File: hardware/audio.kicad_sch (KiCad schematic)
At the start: 21 parts, among them J4 3.5mm stereo, U50 MCP6002

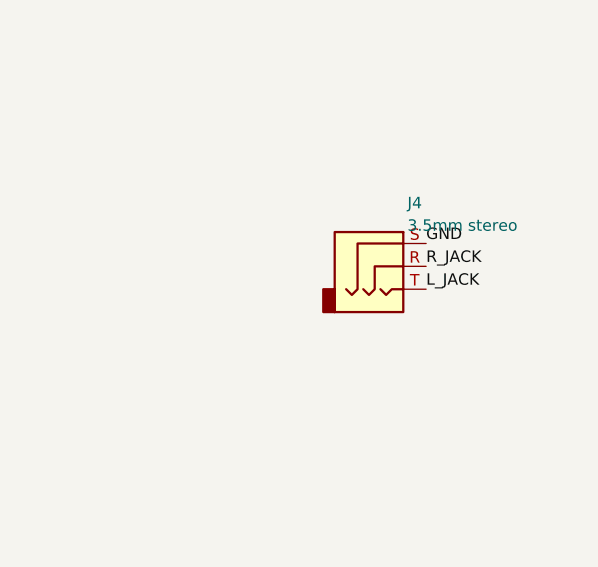
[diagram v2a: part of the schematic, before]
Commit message: BOM cost optimisation against the JLCPCB catalog; schematic-side regulator fix
jlc_price.py prices the BOM via JLCPCB's parts API. Substitutions cut parts+fees
per board from $32.95 to $17.19 on a 10-board run: PSRAM DNP, electrolytic bulk
caps, TF-01A socket, PJ-320D jack, 74HC574, GD25Q128E, 0603 10 uF, basic LED,
preferred MCP6002; U16 decoder deleted (strobes on GPIO), U8 and U15 become
74LVC245s; J3/J5 hand-soldered. Adds the AOTA inductor and VREG_AVDD filter.
PCB needs a relayout; fab/ is stale.

Co-Authored-By: Claude Fable 5.1 <noreply@anthropic.com>
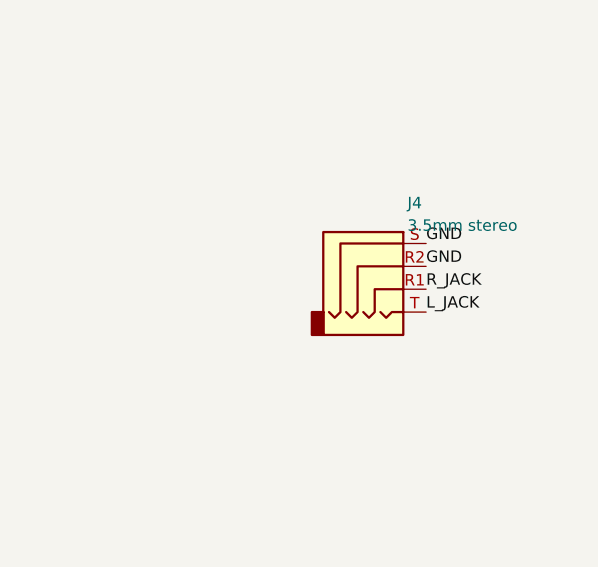
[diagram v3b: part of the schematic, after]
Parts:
- removed J4: 3.5mm stereo, Connector_Audio:Jack_3.5mm_CUI_SJ-3523-SMT_Horizontal, symbol Connector_Audio:AudioJack3
- added J4: 3.5mm stereo, Connector_Audio:Jack_3.5mm_PJ320D_Horizontal, symbol Connector_Audio:AudioJack4
- C80, C81: footprint Capacitor_SMD:C_0805_2012Metric -> Capacitor_SMD:C_0603_1608Metric; LCSC C15850 -> C19702; MPN CL21A106KAYNNNE -> CL10A106KP8NNNC
- U50: LCSC C125816 -> C7377; MPN MCP6002T-E/SN -> MCP6002T-I/SN
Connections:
- net GND: now also J4.R2, J4.S
- net L_JACK: now also J4.T
- net R_JACK: now also J4.R1
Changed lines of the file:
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@@
     (property "Datasheet" "" (at 199.39 110.49 0) (effects (font (size 1.27 1.27)) (justify left) (hide yes)))
     (property "Description" "" (at 199.39 110.49 0) (effects (font (size 1.27 1.27)) (justify left) (hide yes)))
-    (property "MPN" "MCP6002T-E/SN" (at 199.39 110.49 0) (effects (font (size 1.27 1.27)) (justify left) (hide yes)))
-    (property "LCSC" "C125816" (at 199.39 110.49 0) (effects (font (size 1.27 1.27)) (justify left) (hide yes)))
+    (property "MPN" "MCP6002T-I/SN" (at 199.39 110.49 0) (effects (font (size 1.27 1.27)) (justify left) (hide yes)))
+    (property "LCSC" "C7377" (at 199.39 110.49 0) (effects (font (size 1.27 1.27)) (justify left) (hide yes)))
     (pin "1")
     (pin "2")
@@
     (property "Datasheet" "" (at 199.39 170.18 0) (effects (font (size 1.27 1.27)) (justify left) (hide yes)))
     (property "Description" "" (at 199.39 170.18 0) (effects (font (size 1.27 1.27)) (justify left) (hide yes)))
-    (property "MPN" "MCP6002T-E/SN" (at 199.39 170.18 0) (effects (font (size 1.27 1.27)) (justify left) (hide yes)))
-    (property "LCSC" "C125816" (at 199.39 170.18 0) (effects (font (size 1.27 1.27)) (justify left) (hide yes)))
+    (property "MPN" "MCP6002T-I/SN" (at 199.39 170.18 0) (effects (font (size 1.27 1.27)) (justify left) (hide yes)))
+    (property "LCSC" "C7377" (at 199.39 170.18 0) (effects (font (size 1.27 1.27)) (justify left) (hide yes)))
     (pin "1")
     (pin "2")
@@
     (property "Datasheet" "" (at 199.39 229.87 0) (effects (font (size 1.27 1.27)) (justify left) (hide yes)))
     (property "Description" "" (at 199.39 229.87 0) (effects (font (size 1.27 1.27)) (justify left) (hide yes)))
-    (property "MPN" "MCP6002T-E/SN" (at 199.39 229.87 0) (effects (font (size 1.27 1.27)) (justify left) (hide yes)))
-    (property "LCSC" "C125816" (at 199.39 229.87 0) (effects (font (size 1.27 1.27)) (justify left) (hide yes)))
+    (property "MPN" "MCP6002T-I/SN" (at 199.39 229.87 0) (effects (font (size 1.27 1.27)) (justify left) (hide yes)))
+    (property "LCSC" "C7377" (at 199.39 229.87 0) (effects (font (size 1.27 1.27)) (justify left) (hide yes)))
     (pin "1")
     (pin "2")
@@
     (property "Reference" "C80" (at 253.19 102.18 0) (effects (font (size 1.27 1.27)) (justify left)))
     (property "Value" "10u" (at 253.19 104.68 0) (effects (font (size 1.27 1.27)) (justify left)))
-    (property "Footprint" "Capacitor_SMD:C_0805_2012Metric" (at 250.19 110.49 0) (effects (font (size 1.27 1.27)) (justify left) (hide yes)))
+    (property "Footprint" "Capacitor_SMD:C_0603_1608Metric" (at 250.19 110.49 0) (effects (font (size 1.27 1.27)) (justify left) (hide yes)))
     (property "Datasheet" "" (at 250.19 110.49 0) (effects (font (size 1.27 1.27)) (justify left) (hide yes)))
     (property "Description" "" (at 250.19 110.49 0) (effects (font (size 1.27 1.27)) (justify left) (hide yes)))
-    (property "MPN" "CL21A106KAYNNNE" (at 250.19 110.49 0) (effects (font (size 1.27 1.27)) (justify left) (hide yes)))
-    (property "LCSC" "C15850" (at 250.19 110.49 0) (effects (font (size 1.27 1.27)) (justify left) (hide yes)))
+    (property "MPN" "CL10A106KP8NNNC" (at 250.19 110.49 0) (effects (font (size 1.27 1.27)) (justify left) (hide yes)))
+    (property "LCSC" "C19702" (at 250.19 110.49 0) (effects (font (size 1.27 1.27)) (justify left) (hide yes)))
     (pin "1")
     (pin "2")
@@
     (property "Reference" "C81" (at 253.19 161.87 0) (effects (font (size 1.27 1.27)) (justify left)))
     (property "Value" "10u" (at 253.19 164.37 0) (effects (font (size 1.27 1.27)) (justify left)))
-    (property "Footprint" "Capacitor_SMD:C_0805_2012Metric" (at 250.19 170.18 0) (effects (font (size 1.27 1.27)) (justify left) (hide yes)))
+    (property "Footprint" "Capacitor_SMD:C_0603_1608Metric" (at 250.19 170.18 0) (effects (font (size 1.27 1.27)) (justify left) (hide yes)))
     (property "Datasheet" "" (at 250.19 170.18 0) (effects (font (size 1.27 1.27)) (justify left) (hide yes)))
     (property "Description" "" (at 250.19 170.18 0) (effects (font (size 1.27 1.27)) (justify left) (hide yes)))
-    (property "MPN" "CL21A106KAYNNNE" (at 250.19 170.18 0) (effects (font (size 1.27 1.27)) (justify left) (hide yes)))
-    (property "LCSC" "C15850" (at 250.19 170.18 0) (effects (font (size 1.27 1.27)) (justify left) (hide yes)))
+    (property "MPN" "CL10A106KP8NNNC" (at 250.19 170.18 0) (effects (font (size 1.27 1.27)) (justify left) (hide yes)))
+    (property "LCSC" "C19702" (at 250.19 170.18 0) (effects (font (size 1.27 1.27)) (justify left) (hide yes)))
     (pin "1")
     (pin "2")
@@
   (label "R_AC" (at 270.51 166.37 90) (effects (font (size 1.27 1.27)) (justify left bottom)))
   (label "R_JACK" (at 270.51 173.99 270) (effects (font (size 1.27 1.27)) (justify right bottom)))
-  (symbol (lib_id "Connector_Audio:AudioJack3") (at 320.04 139.7 0) (unit 1)
+  (symbol (lib_id "Connector_Audio:AudioJack4") (at 320.04 139.7 0) (unit 1)
     (exclude_from_sim no) (in_bom yes) (on_board yes) (dnp no)
     (property "Reference" "J4" (at 323.04 132.66 0) (effects (font (size 1.27 1.27)) (justify left)))
     (property "Value" "3.5mm stereo" (at 323.04 135.16 0) (effects (font (size 1.27 1.27)) (justify left)))
-    (property "Footprint" "Connector_Audio:Jack_3.5mm_CUI_SJ-3523-SMT_Horizontal" (at 320.04 139.7 0) (effects (font (size 1.27 1.27)) (justify left) (hide yes)))
+    (property "Footprint" "Connector_Audio:Jack_3.5mm_PJ320D_Horizontal" (at 320.04 139.7 0) (effects (font (size 1.27 1.27)) (justify left) (hide yes)))
     (property "Datasheet" "" (at 320.04 139.7 0) (effects (font (size 1.27 1.27)) (justify left) (hide yes)))
     (property "Description" "" (at 320.04 139.7 0) (effects (font (size 1.27 1.27)) (justify left) (hide yes)))
-    (property "MPN" "SJ-3523-SMT-TR" (at 320.04 139.7 0) (effects (font (size 1.27 1.27)) (justify left) (hide yes)))
-    (property "LCSC" "C4991872" (at 320.04 139.7 0) (effects (font (size 1.27 1.27)) (justify left) (hide yes)))
-    (pin "R")
+    (property "MPN" "PJ-320D" (at 320.04 139.7 0) (effects (font (size 1.27 1.27)) (justify left) (hide yes)))
+    (property "LCSC" "C431535" (at 320.04 139.7 0) (effects (font (size 1.27 1.27)) (justify left) (hide yes)))
+    (pin "R1")
+    (pin "R2")
     (pin "S")
     (pin "T")
     (instances (project "tspico-v3" (path "/9088d141-8624-4d5c-91a9-7a3a7a90b3cc/2f11af4c-93bf-47a1-9f9b-ac2a74f731ab" (reference "J4") (unit 1))))
   )
-  (label "L_JACK" (at 325.12 142.24 0) (effects (font (size 1.27 1.27)) (justify left bottom)))
-  (label "R_JACK" (at 325.12 139.70 0) (effects (font (size 1.27 1.27)) (justify left bottom)))
+  (label "L_JACK" (at 325.12 144.78 0) (effects (font (size 1.27 1.27)) (justify left bottom)))
+  (label "R_JACK" (at 325.12 142.24 0) (effects (font (size 1.27 1.27)) (justify left bottom)))
+  (label "GND" (at 325.12 139.70 0) (effects (font (size 1.27 1.27)) (justify left bottom)))
   (label "GND" (at 325.12 137.16 0) (effects (font (size 1.27 1.27)) (justify left bottom)))
   (text "Mix: L = AY A + AY B/2, R = AY C + AY B/2 done in firmware; SOUND_2068 added to both channels here." (exclude_from_sim no) (at 40 215 0) (effects (font (size 1.5 1.5)) (justify left bottom)))
